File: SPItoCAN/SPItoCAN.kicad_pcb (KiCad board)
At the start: 2 copper layers, 30.7 x 22.1 mm, 30 parts, among them J1 CONN_01x02, J2 CONN_01x02, J3 CONN_01x02, J4 Conn_01x07, U1 TJA1051T-E, U2 MCP2515-xSO, Y1 Crystal_8MHz

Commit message: Further updated PCB to meet JLCPCB capabilites. Pushing etc. Tach files
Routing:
- net VCC: track 36.8 -> 38.3 mm
- net /TXCAN: track 12.3 -> 11.1 mm
- net /SI: track 10.5 -> 9.98 mm
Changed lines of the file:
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@@
       (drillshape 0)
       (scaleselection 1)
-      (outputdirectory "gerber/test2")
+      (outputdirectory "gerber/test23")
     )
   )
@@
     )
     (fp_line (start 0 5.885) (end 3.86 5.885) (layer "F.SilkS") (width 0.12))
-    (fp_line (start 3.86 5.885) (end 3.86 5.64) (layer "F.SilkS") (width 0.12))
-    (fp_line (start -3.86 -5.885) (end -3.86 -5.64) (layer "F.SilkS") (width 0.12))
-    (fp_line (start 0 -5.885) (end -3.86 -5.885) (layer "F.SilkS") (width 0.12))
-    (fp_line (start -3.86 -5.64) (end -5.675 -5.64) (layer "F.SilkS") (width 0.12))
-    (fp_line (start 0 -5.885) (end 3.86 -5.885) (layer "F.SilkS") (width 0.12))
-    (fp_line (start 0 5.885) (end -3.86 5.885) (layer "F.SilkS") (width 0.12))
-    (fp_line (start 3.86 -5.885) (end 3.86 -5.64) (layer "F.SilkS") (width 0.12))
+    (fp_line (start 3.86 5.885) (end 3.86 5.64) (layer "F.SilkS") (width 0.155))
+    (fp_line (start -3.86 -5.885) (end -3.86 -5.64) (layer "F.SilkS") (width 0.155))
+    (fp_line (start 0 -5.885) (end -3.86 -5.885) (layer "F.SilkS") (width 0.155))
+    (fp_line (start -3.86 -5.64) (end -5.675 -5.64) (layer "F.SilkS") (width 0.155))
+    (fp_line (start 0 -5.885) (end 3.86 -5.885) (layer "F.SilkS") (width 0.155))
+    (fp_line (start 0 5.885) (end -3.86 5.885) (layer "F.SilkS") (width 0.155))
+    (fp_line (start 3.86 -5.885) (end 3.86 -5.64) (layer "F.SilkS") (width 0.155))
     (fp_line (start -3.86 5.885) (end -3.86 5.64) (layer "F.SilkS") (width 0.12))
     (fp_line (start 5.93 -6.02) (end -5.93 -6.02) (layer "F.CrtYd") (width 0.05))
@@
     (effects (font (size 1 1) (thickness 0.16)))
   )
-  (segment (start 36.159 32.6794) (end 36.159 32.3744) (width 0.25) (layer "F.Cu") (net 1))
   (via (at 26.924 19.3294) (size 0.9) (drill 0.4) (layers "F.Cu" "B.Cu") (free) (net 1))
   (via (at 18.554 26.6794) (size 0.9) (drill 0.4) (layers "F.Cu" "B.Cu") (free) (net 1))
@@
   (segment (start 23.114 32.7914) (end 25.654 32.7914) (width 0.25) (layer "F.Cu") (net 2))
   (segment (start 24.654 30.2694) (end 24.664 30.2794) (width 0.25) (layer "F.Cu") (net 2))
-  (segment (start 18.602 30.2794) (end 17.864 30.2794) (width 0.25) (layer "F.Cu") (net 2))
   (segment (start 26.162 32.2834) (end 26.67 32.7914) (width 0.25) (layer "F.Cu") (net 2))
   (segment (start 20.304 29.2294) (end 20.304 26.6594) (width 0.25) (layer "F.Cu") (net 2))
@@
   (segment (start 17.864 30.2794) (end 19.304 30.2794) (width 0.25) (layer "F.Cu") (net 2))
   (segment (start 23.294 30.2694) (end 24.654 30.2694) (width 0.25) (layer "F.Cu") (net 2))
-  (segment (start 23.294 30.2694) (end 23.294 30.6114) (width 0.25) (layer "F.Cu") (net 2))
   (segment (start 33.619 28.9044) (end 33.619 27.7294) (width 0.25) (layer "F.Cu") (net 2))
   (segment (start 19.304 30.2794) (end 19.304 30.2294) (width 0.25) (layer "F.Cu") (net 2))
@@
   (via (at 19.304 30.2794) (size 0.9) (drill 0.4) (layers "F.Cu" "B.Cu") (net 2))
   (via (at 32.773 29.7504) (size 0.9) (drill 0.4) (layers "F.Cu" "B.Cu") (net 2))
-  (segment (start 29.99 32) (end 32.519 29.471) (width 0.25) (layer "B.Cu") (net 2))
-  (segment (start 25.908 32.004) (end 25.412 32.5) (width 0.25) (layer "B.Cu") (net 2))
-  (segment (start 25.912 32) (end 29.99 32) (width 0.25) (layer "B.Cu") (net 2))
-  (segment (start 25.908 32.004) (end 25.912 32) (width 0.25) (layer "B.Cu") (net 2))
-  (segment (start 18.768 30) (end 20.5 30) (width 0.25) (layer "B.Cu") (net 2))
-  (segment (start 25.412 32.5) (end 23 32.5) (width 0.25) (layer "B.Cu") (net 2))
-  (segment (start 20.5 30) (end 23 32.5) (width 0.25) (layer "B.Cu") (net 2))
+  (segment (start 24.8666 30.988) (end 21.336 30.988) (width 0.25) (layer "B.Cu") (net 2))
+  (segment (start 21.336 30.988) (end 20.6274 30.2794) (width 0.25) (layer "B.Cu") (net 2))
+  (segment (start 23 32.5) (end 25.9454 32.5) (width 0.25) (layer "B.Cu") (net 2))
+  (segment (start 26.162 32.2834) (end 30.24 32.2834) (width 0.25) (layer "B.Cu") (net 2))
+  (segment (start 25.9454 32.5) (end 26.162 32.2834) (width 0.25) (layer "B.Cu") (net 2))
+  (segment (start 20.6274 30.2794) (end 19.304 30.2794) (width 0.25) (layer "B.Cu") (net 2))
+  (segment (start 26.162 32.2834) (end 24.8666 30.988) (width 0.25) (layer "B.Cu") (net 2))
+  (segment (start 30.24 32.2834) (end 32.773 29.7504) (width 0.25) (layer "B.Cu") (net 2))
   (segment (start 26.564 30.2794) (end 28.134 30.2794) (width 0.25) (layer "F.Cu") (net 3))
   (segment (start 28.134 30.2794) (end 28.164 30.3094) (width 0.25) (layer "F.Cu") (net 3))
@@
   (segment (start 17.629 25.0294) (end 15.174 25.0294) (width 0.25) (layer "F.Cu") (net 5))
   (segment (start 21.963399 24.1194) (end 20.304 24.1194) (width 0.25) (layer "F.Cu") (net 5))
-  (segment (start 15.174 25.0294) (end 15.004 25.1994) (width 0.25) (layer "F.Cu") (net 5))
   (via (at 22.777272 24.933273) (size 0.9) (drill 0.4) (layers "F.Cu" "B.Cu") (net 5))
   (segment (start 22.777272 27.733272) (end 24 28.956) (width 0.25) (layer "B.Cu") (net 5))
@@
   (segment (start 20.304 21.5794) (end 16.464 21.5794) (width 0.25) (layer "F.Cu") (net 6))
   (segment (start 16.464 21.5794) (end 15.004 20.1194) (width 0.25) (layer "F.Cu") (net 6))
-  (segment (start 22.254 21.7794) (end 20.504 21.7794) (width 0.25) (layer "F.Cu") (net 6))
-  (segment (start 20.504 21.7794) (end 20.304 21.5794) (width 0.25) (layer "F.Cu") (net 6))
+  (segment (start 22.054 21.5794) (end 22.254 21.7794) (width 0.25) (layer "F.Cu") (net 6))
+  (segment (start 20.304 21.5794) (end 22.054 21.5794) (width 0.25) (layer "F.Cu") (net 6))
   (via (at 22.254 21.7794) (size 0.9) (drill 0.4) (layers "F.Cu" "B.Cu") (net 6))
-  (segment (start 22 21.8) (end 22 21.5) (width 0.25) (layer "B.Cu") (net 6))
-  (segment (start 22.7 22.5) (end 22 21.8) (width 0.25) (layer "B.Cu") (net 6))
-  (segment (start 24 22.5) (end 22.7 22.5) (width 0.25) (layer "B.Cu") (net 6))
+  (segment (start 22.9746 22.5) (end 22.254 21.7794) (width 0.25) (layer "B.Cu") (net 6))
+  (segment (start 24 22.5) (end 22.9746 22.5) (width 0.25) (layer "B.Cu") (net 6))
   (segment (start 20.124 23.0294) (end 15.374 23.0294) (width 0.25) (layer "F.Cu") (net 7))
   (segment (start 23.3574 22.8494) (end 20.304 22.8494) (width 0.25) (layer "F.Cu") (net 7))
@@
   (segment (start 21.394 30.2694) (end 21.394 29.406) (width 0.25) (layer "F.Cu") (net 10))
   (segment (start 22.86 27.94) (end 22.86 26.416) (width 0.25) (layer "F.Cu") (net 10))
-  (segment (start 36.004 27.5744) (end 36.159 27.7294) (width 0.25) (layer "F.Cu") (net 11))
   (segment (start 36.159 26.5324) (end 35.306 25.6794) (width 0.25) (layer "F.Cu") (net 11))
-  (segment (start 36.004 26.9799) (end 36.004 27.5744) (width 0.25) (layer "F.Cu") (net 11))
   (segment (start 30.754 27.8794) (end 30.754 27.8094) (width 0.25) (layer "F.Cu") (net 11))
   (segment (start 30.754 27.8094) (end 29.604 26.6594) (width 0.25) (layer "F.Cu") (net 11))
@@
   (segment (start 35.306 25.6794) (end 33.106 27.8794) (width 0.25) (layer "B.Cu") (net 11))
   (segment (start 33.106 27.8794) (end 30.754 27.8794) (width 0.25) (layer "B.Cu") (net 11))
-  (segment (start 30.5 25.8118) (end 30.7848 25.527) (width 0.25) (layer "B.Cu") (net 11))
   (segment (start 30.754 26.182) (end 30.734 26.162) (width 0.25) (layer "B.Cu") (net 11))
   (segment (start 30.754 27.8794) (end 30.754 26.182) (width 0.25) (layer "B.Cu") (net 11))
-  (segment (start 29.714 25.2794) (end 29.604 25.3894) (width 0.25) (layer "F.Cu") (net 12))
   (segment (start 32.554 24.6994) (end 31.864 25.3894) (width 0.25) (layer "F.Cu") (net 12))
   (segment (start 32.349 25.8744) (end 32.349 27.7294) (width 0.25) (layer "F.Cu") (net 12))
@@
   (segment (start 33.254 20.848) (end 33.274 20.828) (width 0.2) (layer "B.Cu") (net 22))
   (segment (start 33.254 22.7794) (end 33.254 20.848) (width 0.2) (layer "B.Cu") (net 22))
-  (segment (start 35.629 15.8544) (end 35.654 15.8294) (width 0.2) (layer "F.Cu") (net 23))
   (segment (start 33.254 15.8544) (end 31.339 17.7694) (width 0.2) (layer "F.Cu") (net 23))
   (segment (start 31.339 17.7694) (end 31.244 17.7694) (width 0.2) (layer "F.Cu") (net 23))
   (segment (start 31.244 17.7694) (end 29.604 17.7694) (width 0.2) (layer "F.Cu") (net 23))
   (segment (start 33.254 15.8544) (end 35.629 15.8544) (width 0.2) (layer "F.Cu") (net 23))
-  (segment (start 35.629 15.8044) (end 35.654 15.8294) (width 0.25) (layer "F.Cu") (net 23))
   (via (at 31.244 17.7694) (size 0.9) (drill 0.4) (layers "F.Cu" "B.Cu") (net 23))
   (segment (start 31.244 17.7694) (end 29.4746 17.7694) (width 0.2) (layer "B.Cu") (net 23))

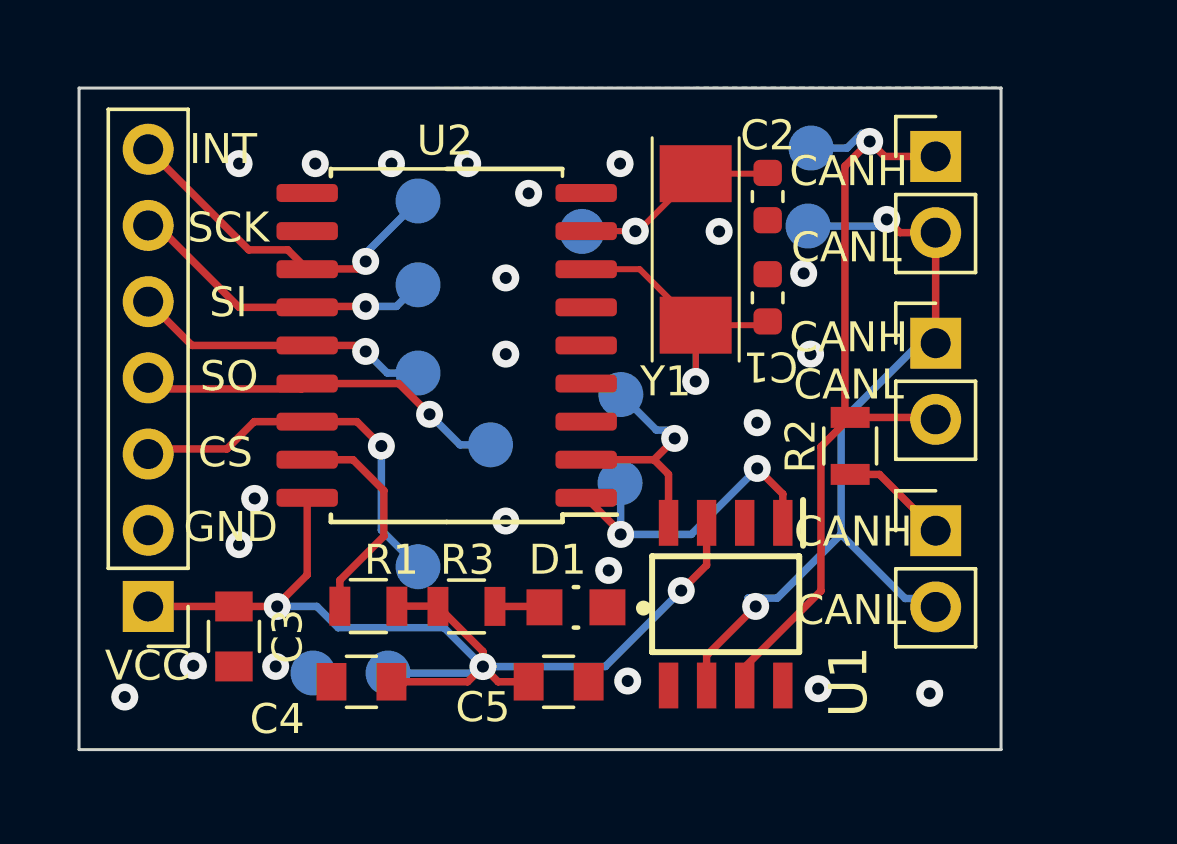
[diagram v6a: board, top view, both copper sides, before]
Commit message: Final updates and gerber for board production
Updated so board fits into breadboard and other misc. updates before generating gerbers
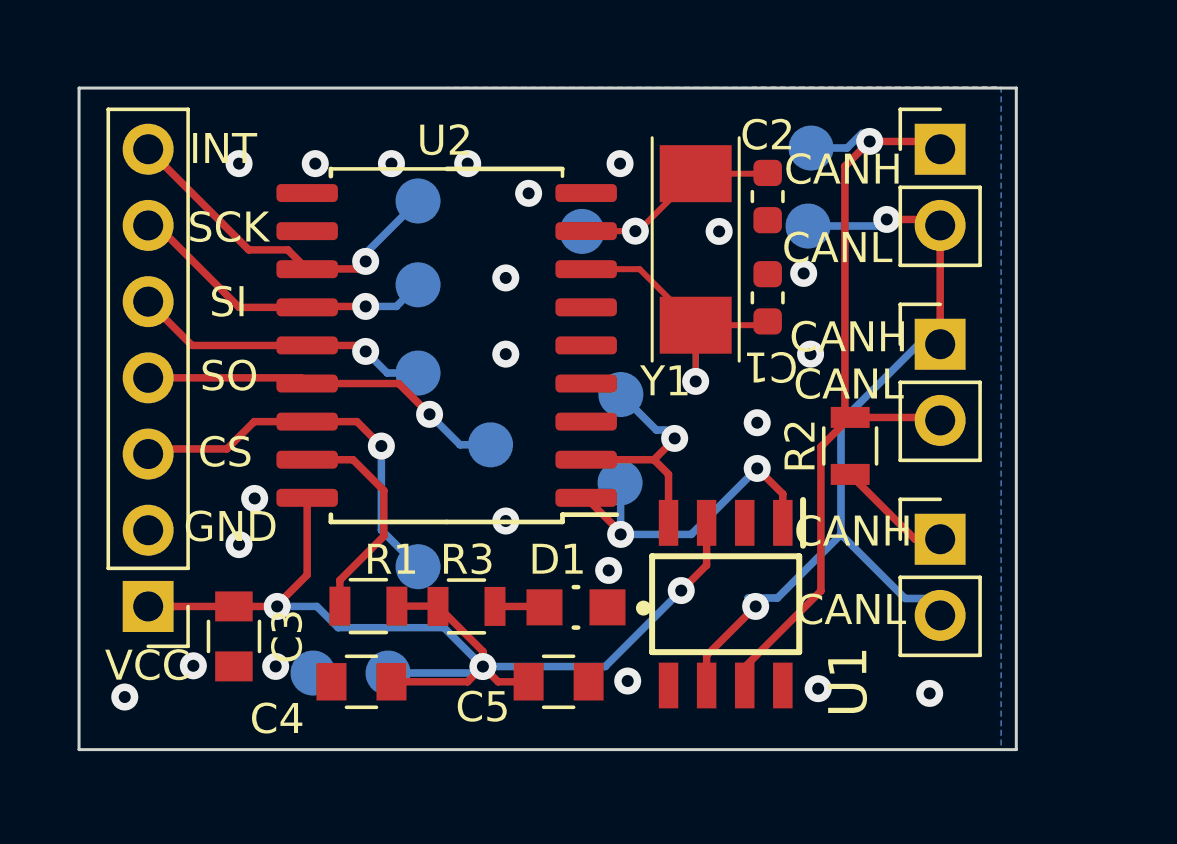
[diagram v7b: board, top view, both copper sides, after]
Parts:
- moved J1 0.32 mm to (41.4, 28.0)
- moved J2 0.28 mm to (41.4, 15.0)
- moved J3 0.15 mm to (41.4, 21.5)
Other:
- board size 30.7 x 22.1 mm -> 31.2 x 22.1 mm
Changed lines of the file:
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@@
       (drillshape 0)
       (scaleselection 1)
-      (outputdirectory "gerber/test23")
+      (outputdirectory "gerber/board_30jan23")
     )
   )
@@
   )
   (footprint "footprints:PinHeader_1x02_P2.54mm_Vertical" (layer "F.Cu")
-    (at 41.254 27.7544)
+    (at 41.404 28.0394)
     (descr "Through hole straight pin header, 1x02, 2.54mm pitch, single row")
     (tags "Through hole pin header THT 1x02 2.54mm single row")
@@
     (pad "6" thru_hole oval (at 0 12.7 180) (size 1.7 1.7) (drill 1) (layers *.Cu *.Mask)
       (net 8 "/SCK") (pinfunction "6") (pintype "passive"))
-    (pad "7" thru_hole oval (at 0 15.24 180) (size 1.7 1.7) (drill 1) (layers *.Cu *.Mask)
+    (pad "7" thru_hole oval locked (at 0 15.24 180) (size 1.7 1.7) (drill 1) (layers *.Cu *.Mask)
       (net 9 "/INT") (pinfunction "7") (pintype "passive"))
     (model "${KICAD6_3DMODEL_DIR}/Connector_PinHeader_2.54mm.3dshapes/PinHeader_1x07_P2.54mm_Vertical.wrl"
@@
   )
   (footprint "footprints:PinHeader_1x02_P2.54mm_Vertical" (layer "F.Cu")
-    (at 41.254 15.2794)
+    (at 41.404 15.0394)
     (descr "Through hole straight pin header, 1x02, 2.54mm pitch, single row")
     (tags "Through hole pin header THT 1x02 2.54mm single row")
@@
   )
   (footprint "footprints:PinHeader_1x02_P2.54mm_Vertical" (layer "F.Cu")
-    (at 41.254 21.5044)
+    (at 41.404 21.5394)
     (descr "Through hole straight pin header, 1x02, 2.54mm pitch, single row")
     (tags "Through hole pin header THT 1x02 2.54mm single row")
@@
       (net 1 "GND") (pintype "input"))
   )
-  (gr_rect (start 12.7 13) (end 43.434 35.052) (layer "Edge.Cuts") (width 0.1) (fill none))
+  (gr_rect (start 12.7 13) (end 43.942 35.052) (layer "Edge.Cuts") (width 0.1) (fill none))
   (gr_text "Olin Baja - 22-23" (at 23.876 14.224) (layer "B.SilkS")
     (effects (font (size 1 1) (thickness 0.25)) (justify mirror))
@@
     (effects (font (size 1 1) (thickness 0.16)))
   )
-  (gr_text "CANH" (at 38.354 15.7734) (layer "F.SilkS")
+  (gr_text "CANH" (at 38.1762 15.7226) (layer "F.SilkS")
     (effects (font (size 1 1) (thickness 0.16)))
   )
@@
     (effects (font (size 1 1) (thickness 0.16)))
   )
-  (gr_text "CANL" (at 38.2778 18.3134) (layer "F.SilkS")
+  (gr_text "CANL" (at 37.973 18.3388) (layer "F.SilkS")
     (effects (font (size 1 1) (thickness 0.16)))
   )
@@
   (segment (start 26.564 30.2794) (end 28.134 30.2794) (width 0.25) (layer "F.Cu") (net 3))
   (segment (start 28.134 30.2794) (end 28.164 30.3094) (width 0.25) (layer "F.Cu") (net 3))
-  (segment (start 38.404 25.8794) (end 39.379 25.8794) (width 0.25) (layer "F.Cu") (net 4))
-  (segment (start 39.379 25.8794) (end 41.254 27.7544) (width 0.25) (layer "F.Cu") (net 4))
+  (segment (start 40.564 28.0394) (end 41.404 28.0394) (width 0.25) (layer "F.Cu") (net 4))
+  (segment (start 38.404 25.8794) (end 40.564 28.0394) (width 0.25) (layer "F.Cu") (net 4))
   (segment (start 20.304 24.1194) (end 18.539 24.1194) (width 0.25) (layer "F.Cu") (net 5))
   (segment (start 22.777272 24.933273) (end 21.963399 24.1194) (width 0.25) (layer "F.Cu") (net 5))
@@
   (segment (start 22.9746 22.5) (end 22.254 21.7794) (width 0.25) (layer "B.Cu") (net 6))
   (segment (start 24 22.5) (end 22.9746 22.5) (width 0.25) (layer "B.Cu") (net 6))
-  (segment (start 20.124 23.0294) (end 15.374 23.0294) (width 0.25) (layer "F.Cu") (net 7))
+  (segment (start 20.114 22.6594) (end 15.004 22.6594) (width 0.25) (layer "F.Cu") (net 7))
   (segment (start 23.3574 22.8494) (end 20.304 22.8494) (width 0.25) (layer "F.Cu") (net 7))
   (segment (start 24.384 23.876) (end 23.3574 22.8494) (width 0.25) (layer "F.Cu") (net 7))
-  (segment (start 20.304 22.8494) (end 20.124 23.0294) (width 0.25) (layer "F.Cu") (net 7))
+  (segment (start 20.304 22.8494) (end 20.114 22.6594) (width 0.25) (layer "F.Cu") (net 7))
   (segment (start 15.374 23.0294) (end 15.004 22.6594) (width 0.25) (layer "F.Cu") (net 7))
   (via (at 24.384 23.876) (size 0.9) (drill 0.4) (layers "F.Cu" "B.Cu") (net 7))
@@
   (segment (start 19.659 18.3944) (end 18.359 18.3944) (width 0.25) (layer "F.Cu") (net 9))
   (segment (start 20.304 19.0394) (end 19.659 18.3944) (width 0.25) (layer "F.Cu") (net 9))
-  (segment (start 18.359 18.3944) (end 15.004 15.0394) (width 0.25) (layer "F.Cu") (net 9))
+  (segment locked (start 18.359 18.3944) (end 15.004 15.0394) (width 0.25) (layer "F.Cu") (net 9))
   (segment (start 22.004 19.0294) (end 20.314 19.0294) (width 0.25) (layer "F.Cu") (net 9))
   (segment (start 22.254 18.7794) (end 22.004 19.0294) (width 0.25) (layer "F.Cu") (net 9))
@@
   (segment (start 31.9438 24.4) (end 30.7594 23.2156) (width 0.25) (layer "B.Cu") (net 12))
   (segment (start 32.3 24.4) (end 31.9438 24.4) (width 0.25) (layer "B.Cu") (net 12))
+  (segment (start 39.624 17.3794) (end 41.204 17.3794) (width 0.25) (layer "F.Cu") (net 20))
   (segment (start 35.254 30.2794) (end 33.619 31.9144) (width 0.25) (layer "F.Cu") (net 20))
-  (segment (start 41.254 17.8194) (end 41.254 21.5044) (width 0.25) (layer "F.Cu") (net 20))
-  (segment (start 40.064 17.8194) (end 41.254 17.8194) (width 0.25) (layer "F.Cu") (net 20))
+  (segment (start 41.404 21.5394) (end 41.404 17.5794) (width 0.25) (layer "F.Cu") (net 20))
   (segment (start 33.619 31.9144) (end 33.619 32.6794) (width 0.25) (layer "F.Cu") (net 20))
-  (segment (start 39.624 17.3794) (end 40.064 17.8194) (width 0.25) (layer "F.Cu") (net 20))
+  (segment (start 41.204 17.3794) (end 41.404 17.5794) (width 0.25) (layer "F.Cu") (net 20))
   (via (at 35.254 30.2794) (size 0.9) (drill 0.4) (layers "F.Cu" "B.Cu") (net 20))
   (via (at 39.624 17.3794) (size 0.9) (drill 0.4) (layers "F.Cu" "B.Cu") (net 20))
@@
   (segment (start 41 21.225) (end 38.1 24.125) (width 0.25) (layer "B.Cu") (net 20))
   (segment (start 40.23625 30.015) (end 41 30.015) (width 0.25) (layer "B.Cu") (net 20))
-  (segment (start 39.554 15.2794) (end 41.254 15.2794) (width 0.25) (layer "F.Cu") (net 21))
   (segment (start 34.889 32.6794) (end 34.889 32.302649) (width 0.25) (layer "F.Cu") (net 21))
   (segment (start 37.429 29.762649) (end 37.429 24.9544) (width 0.25) (layer "F.Cu") (net 21))
-  (segment (start 38.404 23.9794) (end 41.189 23.9794) (width 0.25) (layer "F.Cu") (net 21))
+  (segment (start 39.054 14.7794) (end 41.144 14.7794) (width 0.25) (layer "F.Cu") (net 21))
+  (segment (start 38.404 23.9794) (end 41.304 23.9794) (width 0.25) (layer "F.Cu") (net 21))
   (segment (start 37.429 24.9544) (end 38.404 23.9794) (width 0.25) (layer "F.Cu") (net 21))
   (segment (start 38.229 23.8044) (end 38.404 23.9794) (width 0.25) (layer "F.Cu") (net 21))
   (segment (start 34.889 32.302649) (end 37.429 29.762649) (width 0.25) (layer "F.Cu") (net 21))
   (segment (start 38.229 15.6044) (end 38.229 23.8044) (width 0.25) (layer "F.Cu") (net 21))
-  (segment (start 39.054 14.7794) (end 39.554 15.2794) (width 0.25) (layer "F.Cu") (net 21))
   (segment (start 39.054 14.7794) (end 38.229 15.6044) (width 0.25) (layer "F.Cu") (net 21))
   (segment (start 41.189 23.9794) (end 41.254 24.0444) (width 0.25) (layer "F.Cu") (net 21))
   (segment (start 34.889 32.6794) (end 34.889 33.056151) (width 0.25) (layer "F.Cu") (net 21))
+  (segment (start 41.304 23.9794) (end 41.404 24.0794) (width 0.25) (layer "F.Cu") (net 21))
+  (segment (start 41.144 14.7794) (end 41.404 15.0394) (width 0.25) (layer "F.Cu") (net 21))
   (via (at 39.054 14.7794) (size 0.9) (drill 0.4) (layers "F.Cu" "B.Cu") (net 21))
   (segment (start 38.3 15) (end 37.1 15) (width 0.25) (layer "B.Cu") (net 21))
@@
     (polygon
       (pts
-        (xy 43.434 35.052)
+        (xy 43.942 35.052)
         (xy 12.7 35.052)
         (xy 12.7 13)
-        (xy 43.434 13)
+        (xy 43.942 13)
       )
     )
